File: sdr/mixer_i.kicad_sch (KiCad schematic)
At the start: 1 part, among them U7 74LVC1G66

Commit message: Complete layout
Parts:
- added C11: 10n, Capacitor_SMD:C_0402_1005Metric, symbol Device:C
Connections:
- net +3.3V: now also C11.1
- net GND: now also C11.2
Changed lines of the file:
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@@
 (kicad_sch (version 20230121) (generator eeschema)
   (paper "A4")
-  (wire (pts (xy 180.34 80.518) (xy 180.34 82.804))
+  (junction (at 180.34 82.55) (diameter 0) (color 0 0 0 0)
+  )
+  (junction (at 186.69 92.71) (diameter 0) (color 0 0 0 0)
+  )
+  (wire (pts (xy 180.34 80.01) (xy 180.34 82.55))
     (stroke (width 0) (type default))
   )
-  (wire (pts (xy 164.592 87.884) (xy 166.624 87.884))
+  (wire (pts (xy 165.1 87.63) (xy 166.37 87.63))
     (stroke (width 0) (type default))
   )
-  (wire (pts (xy 180.34 82.804) (xy 174.244 82.804))
+  (wire (pts (xy 180.34 82.55) (xy 173.99 82.55))
     (stroke (width 0) (type default))
   )
-  (wire (pts (xy 164.592 91.694) (xy 166.624 91.694))
+  (wire (pts (xy 165.1 91.44) (xy 166.37 91.44))
     (stroke (width 0) (type default))
   )
-  (wire (pts (xy 179.324 87.884) (xy 180.594 87.884))
+  (wire (pts (xy 173.99 92.71) (xy 186.69 92.71))
     (stroke (width 0) (type default))
   )
-  (wire (pts (xy 174.244 82.804) (xy 174.244 84.074))
+  (wire (pts (xy 180.34 82.55) (xy 180.34 85.09))
     (stroke (width 0) (type default))
   )
-  (hierarchical_label "LO" (shape input) (at 164.592 91.694 180) (fields_autoplaced)
+  (wire (pts (xy 179.07 87.63) (xy 180.34 87.63))
+    (stroke (width 0) (type default))
+  )
+  (wire (pts (xy 186.69 85.09) (xy 180.34 85.09))
+    (stroke (width 0) (type default))
+  )
+  (wire (pts (xy 173.99 91.44) (xy 173.99 92.71))
+    (stroke (width 0) (type default))
+  )
+  (wire (pts (xy 173.99 82.55) (xy 173.99 83.82))
+    (stroke (width 0) (type default))
+  )
+  (hierarchical_label "LO" (shape input) (at 165.1 91.44 180) (fields_autoplaced)
     (effects (font (size 1.27 1.27)) (justify right))
   )
-  (hierarchical_label "RF" (shape input) (at 164.592 87.884 180) (fields_autoplaced)
+  (hierarchical_label "RF" (shape input) (at 165.1 87.63 180) (fields_autoplaced)
     (effects (font (size 1.27 1.27)) (justify right))
   )
-  (hierarchical_label "IF" (shape input) (at 180.594 87.884 0) (fields_autoplaced)
+  (hierarchical_label "IF" (shape input) (at 180.34 87.63 0) (fields_autoplaced)
     (effects (font (size 1.27 1.27)) (justify left))
   )
-  (symbol (lib_id "power:+3.3V") (at 180.34 80.518 0) (unit 1)
+  (symbol (lib_id "power:+3.3V") (at 180.34 80.01 0) (unit 1)
     (in_bom yes) (on_board yes) (dnp no) (fields_autoplaced)
-    (property "Reference" "#PWR057" (at 180.34 84.328 0)
+    (property "Reference" "#PWR057" (at 180.34 83.82 0)
       (effects (font (size 1.27 1.27)) hide)
     )
-    (property "Value" "+3.3V" (at 180.34 74.93 0)
+    (property "Value" "+3.3V" (at 180.34 74.422 0)
       (effects (font (size 1.27 1.27)))
     )
-    (property "Footprint" "" (at 180.34 80.518 0)
+    (property "Footprint" "" (at 180.34 80.01 0)
       (effects (font (size 1.27 1.27)) hide)
     )
-    (property "Datasheet" "" (at 180.34 80.518 0)
+    (property "Datasheet" "" (at 180.34 80.01 0)
       (effects (font (size 1.27 1.27)) hide)
     )
@@
     )
   )
-  (symbol (lib_id "74xGxx:74LVC1G66") (at 172.974 87.884 0) (unit 1)
-    (in_bom yes) (on_board yes) (dnp no) (fields_autoplaced)
-    (property "Reference" "U7" (at 172.974 78.994 0)
+  (symbol (lib_id "74xGxx:74LVC1G66") (at 172.72 87.63 0) (unit 1)
+    (in_bom yes) (on_board yes) (dnp no)
+    (property "Reference" "U7" (at 172.72 78.74 0)
       (effects (font (size 1.27 1.27)))
     )
-    (property "Value" "74LVC1G66" (at 172.974 81.534 0)
+    (property "Value" "74LVC1G66" (at 172.72 81.28 0)
       (effects (font (size 1.27 1.27)))
     )
-    (property "Footprint" "Package_TO_SOT_SMD:SOT-353_SC-70-5" (at 172.974 87.884 0)
+    (property "Footprint" "Package_TO_SOT_SMD:SOT-353_SC-70-5" (at 172.72 87.63 0)
       (effects (font (size 1.27 1.27)) hide)
     )
-    (property "Datasheet" "http://www.ti.com/lit/ds/symlink/sn74lvc1g66.pdf" (at 172.974 87.884 0)
+    (property "Datasheet" "http://www.ti.com/lit/ds/symlink/sn74lvc1g66.pdf" (at 172.72 87.63 0)
       (effects (font (size 1.27 1.27)) hide)
     )
@@
     )
   )
-  (symbol (lib_id "power:GND") (at 174.244 91.694 0) (unit 1)
+  (symbol (lib_id "power:GND") (at 186.69 92.71 0) (unit 1)
     (in_bom yes) (on_board yes) (dnp no) (fields_autoplaced)
-    (property "Reference" "#PWR044" (at 174.244 98.044 0)
+    (property "Reference" "#PWR044" (at 186.69 99.06 0)
       (effects (font (size 1.27 1.27)) hide)
     )
-    (property "Value" "GND" (at 174.244 96.139 0)
+    (property "Value" "GND" (at 186.69 97.155 0)
       (effects (font (size 1.27 1.27)))
     )
-    (property "Footprint" "" (at 174.244 91.694 0)
+    (property "Footprint" "" (at 186.69 92.71 0)
       (effects (font (size 1.27 1.27)) hide)
     )
-    (property "Datasheet" "" (at 174.244 91.694 0)
+    (property "Datasheet" "" (at 186.69 92.71 0)
       (effects (font (size 1.27 1.27)) hide)
     )
@@
         )
       )
+    )
+  )
+  (symbol (lib_id "Device:C") (at 186.69 88.9 0) (unit 1)
+    (in_bom yes) (on_board yes) (dnp no) (fields_autoplaced)
+    (property "Reference" "C11" (at 190.5 87.6299 0)
+      (effects (font (size 1.27 1.27)) (justify left))
+    )
+    (property "Value" "10n" (at 190.5 90.1699 0)
+      (effects (font (size 1.27 1.27)) (justify left))
+    )
+    (property "Footprint" "Capacitor_SMD:C_0402_1005Metric" (at 187.6552 92.71 0)
+      (effects (font (size 1.27 1.27)) hide)
+    )
+    (property "Datasheet" "~" (at 186.69 88.9 0)
+      (effects (font (size 1.27 1.27)) hide)
+    )
+    (pin "1")
+    (pin "2")
+    (instances
+      (project "sdr"
+        (path "/ee974380-b45b-4b16-8475-50e4e51dc6cf/ad7b2242-3b39-40b3-b2e9-d6ea800dea9e"
+          (reference "C11") (unit 1)
+        )
+        (path "/ee974380-b45b-4b16-8475-50e4e51dc6cf/cebbb4d4-df0b-4a29-b2b2-0c76d3bf10e4"
+          (reference "C28") (unit 1)
+        )
+        (path "/ee974380-b45b-4b16-8475-50e4e51dc6cf/ae3469ea-e61f-4c82-bce0-cc247848c762"
+          (reference "C29") (unit 1)
+        )
+      )

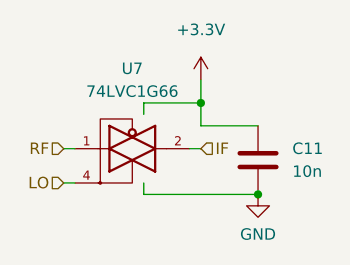
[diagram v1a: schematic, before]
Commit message: Update the via size. Reduce footprints outside board.
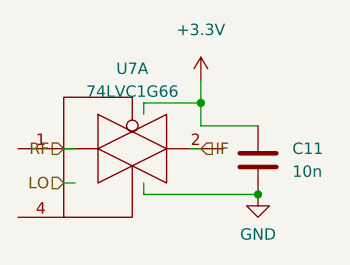
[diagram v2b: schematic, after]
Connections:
- net +3.3V: no longer U7.5 (VCC)
- net GND: no longer U7.3 (GND)
- net IF: no longer U7.2
- net LO: no longer U7.4
- net RF: no longer U7.1
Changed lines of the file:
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@@
     (pin "1")
     (pin "2")
+    (pin "4")
     (pin "3")
-    (pin "4")
     (pin "5")
     (instances

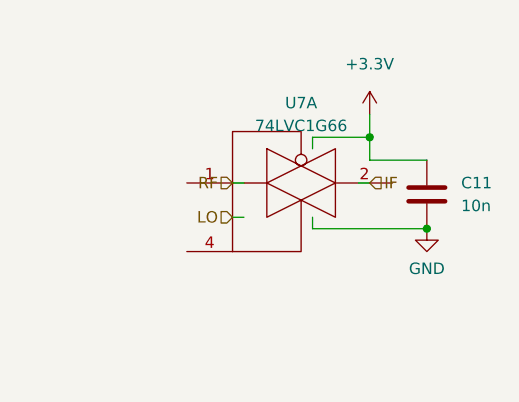
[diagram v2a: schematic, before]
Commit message: Convert to a 4-layer board.
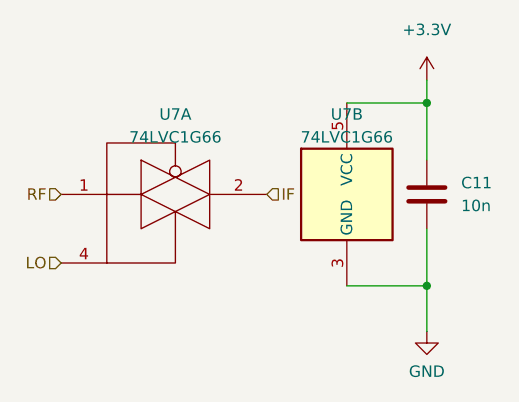
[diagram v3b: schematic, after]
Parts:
- added unit 2 of U7
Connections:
- net +3.3V: now also U7.5 (VCC)
- net GND: now also U7.3 (GND)
- net IF: now also U7.2
- net LO: now also U7.4
- net RF: now also U7.1
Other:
- moved on the sheet: U7A
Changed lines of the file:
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@@
 (kicad_sch (version 20230121) (generator eeschema)
   (paper "A4")
-  (junction (at 180.34 82.55) (diameter 0) (color 0 0 0 0)
+  (junction (at 186.69 78.74) (diameter 0) (color 0 0 0 0)
   )
-  (junction (at 186.69 92.71) (diameter 0) (color 0 0 0 0)
+  (junction (at 186.69 99.06) (diameter 0) (color 0 0 0 0)
   )
-  (wire (pts (xy 180.34 80.01) (xy 180.34 82.55))
+  (wire (pts (xy 186.69 76.2) (xy 186.69 78.74))
     (stroke (width 0) (type default))
   )
-  (wire (pts (xy 165.1 87.63) (xy 166.37 87.63))
+  (wire (pts (xy 177.8 99.06) (xy 186.69 99.06))
     (stroke (width 0) (type default))
   )
-  (wire (pts (xy 180.34 82.55) (xy 173.99 82.55))
+  (wire (pts (xy 186.69 78.74) (xy 186.69 85.09))
     (stroke (width 0) (type default))
   )
-  (wire (pts (xy 165.1 91.44) (xy 166.37 91.44))
+  (wire (pts (xy 177.8 78.74) (xy 186.69 78.74))
     (stroke (width 0) (type default))
   )
-  (wire (pts (xy 173.99 92.71) (xy 186.69 92.71))
+  (wire (pts (xy 186.69 104.14) (xy 186.69 99.06))
     (stroke (width 0) (type default))
   )
-  (wire (pts (xy 180.34 82.55) (xy 180.34 85.09))
+  (wire (pts (xy 186.69 99.06) (xy 186.69 92.71))
     (stroke (width 0) (type default))
   )
-  (wire (pts (xy 179.07 87.63) (xy 180.34 87.63))
-    (stroke (width 0) (type default))
-  )
-  (wire (pts (xy 186.69 85.09) (xy 180.34 85.09))
-    (stroke (width 0) (type default))
-  )
-  (wire (pts (xy 173.99 91.44) (xy 173.99 92.71))
-    (stroke (width 0) (type default))
-  )
-  (wire (pts (xy 173.99 82.55) (xy 173.99 83.82))
-    (stroke (width 0) (type default))
-  )
-  (hierarchical_label "LO" (shape input) (at 165.1 91.44 180) (fields_autoplaced)
+  (hierarchical_label "LO" (shape input) (at 146.05 96.52 180) (fields_autoplaced)
     (effects (font (size 1.27 1.27)) (justify right))
   )
-  (hierarchical_label "RF" (shape input) (at 165.1 87.63 180) (fields_autoplaced)
+  (hierarchical_label "RF" (shape input) (at 146.05 88.9 180) (fields_autoplaced)
     (effects (font (size 1.27 1.27)) (justify right))
   )
-  (hierarchical_label "IF" (shape input) (at 180.34 87.63 0) (fields_autoplaced)
+  (hierarchical_label "IF" (shape input) (at 168.91 88.9 0) (fields_autoplaced)
     (effects (font (size 1.27 1.27)) (justify left))
   )
-  (symbol (lib_id "power:+3.3V") (at 180.34 80.01 0) (unit 1)
+  (symbol (lib_id "power:+3.3V") (at 186.69 76.2 0) (unit 1)
     (in_bom yes) (on_board yes) (dnp no) (fields_autoplaced)
-    (property "Reference" "#PWR057" (at 180.34 83.82 0)
+    (property "Reference" "#PWR057" (at 186.69 80.01 0)
       (effects (font (size 1.27 1.27)) hide)
     )
-    (property "Value" "+3.3V" (at 180.34 74.422 0)
+    (property "Value" "+3.3V" (at 186.69 70.612 0)
       (effects (font (size 1.27 1.27)))
     )
-    (property "Footprint" "" (at 180.34 80.01 0)
+    (property "Footprint" "" (at 186.69 76.2 0)
       (effects (font (size 1.27 1.27)) hide)
     )
-    (property "Datasheet" "" (at 180.34 80.01 0)
+    (property "Datasheet" "" (at 186.69 76.2 0)
       (effects (font (size 1.27 1.27)) hide)
     )
@@
     )
   )
-  (symbol (lib_id "74xGxx:74LVC1G66") (at 172.72 87.63 0) (unit 1)
+  (symbol (lib_id "74xGxx:74LVC1G66") (at 158.75 88.9 0) (unit 1)
     (in_bom yes) (on_board yes) (dnp no)
-    (property "Reference" "U7" (at 172.72 78.74 0)
+    (property "Reference" "U7" (at 158.75 80.01 0)
       (effects (font (size 1.27 1.27)))
     )
-    (property "Value" "74LVC1G66" (at 172.72 81.28 0)
+    (property "Value" "74LVC1G66" (at 158.75 82.55 0)
       (effects (font (size 1.27 1.27)))
     )
-    (property "Footprint" "Package_TO_SOT_SMD:SOT-353_SC-70-5" (at 172.72 87.63 0)
+    (property "Footprint" "Package_TO_SOT_SMD:SOT-353_SC-70-5" (at 158.75 88.9 0)
       (effects (font (size 1.27 1.27)) hide)
     )
-    (property "Datasheet" "http://www.ti.com/lit/ds/symlink/sn74lvc1g66.pdf" (at 172.72 87.63 0)
+    (property "Datasheet" "http://www.ti.com/lit/ds/symlink/sn74lvc1g66.pdf" (at 158.75 88.9 0)
       (effects (font (size 1.27 1.27)) hide)
     )
@@
     )
   )
-  (symbol (lib_id "power:GND") (at 186.69 92.71 0) (unit 1)
+  (symbol (lib_id "power:GND") (at 186.69 104.14 0) (unit 1)
     (in_bom yes) (on_board yes) (dnp no) (fields_autoplaced)
-    (property "Reference" "#PWR044" (at 186.69 99.06 0)
+    (property "Reference" "#PWR044" (at 186.69 110.49 0)
       (effects (font (size 1.27 1.27)) hide)
     )
-    (property "Value" "GND" (at 186.69 97.155 0)
+    (property "Value" "GND" (at 186.69 108.585 0)
       (effects (font (size 1.27 1.27)))
     )
-    (property "Footprint" "" (at 186.69 92.71 0)
+    (property "Footprint" "" (at 186.69 104.14 0)
       (effects (font (size 1.27 1.27)) hide)
     )
-    (property "Datasheet" "" (at 186.69 92.71 0)
+    (property "Datasheet" "" (at 186.69 104.14 0)
       (effects (font (size 1.27 1.27)) hide)
     )
@@
         )
       )
+    )
+  )
+  (symbol (lib_id "74xGxx:74LVC1G66") (at 177.8 88.9 0) (unit 2)
+    (in_bom yes) (on_board yes) (dnp no)
+    (property "Reference" "U7" (at 177.8 80.01 0)
+      (effects (font (size 1.27 1.27)))
+    )
+    (property "Value" "74LVC1G66" (at 177.8 82.55 0)
+      (effects (font (size 1.27 1.27)))
+    )
+    (property "Footprint" "Package_TO_SOT_SMD:SOT-353_SC-70-5" (at 177.8 88.9 0)
+      (effects (font (size 1.27 1.27)) hide)
+    )
+    (property "Datasheet" "http://www.ti.com/lit/ds/symlink/sn74lvc1g66.pdf" (at 177.8 88.9 0)
+      (effects (font (size 1.27 1.27)) hide)
+    )
+    (pin "1")
+    (pin "2")
+    (pin "4")
+    (pin "3")
+    (pin "5")
+    (instances
+      (project "sdr"
+        (path "/ee974380-b45b-4b16-8475-50e4e51dc6cf/cebbb4d4-df0b-4a29-b2b2-0c76d3bf10e4"
+          (reference "U7") (unit 2)
+        )
+        (path "/ee974380-b45b-4b16-8475-50e4e51dc6cf/ae3469ea-e61f-4c82-bce0-cc247848c762"
+          (reference "U11") (unit 2)
+        )
+      )
